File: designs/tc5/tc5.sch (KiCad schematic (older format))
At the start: 9 parts, among them J1001 SSM-104-L-SV, U1001 MCP6001-OT

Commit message: Add component for board edges, generate report
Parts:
- added BRD1: SYM_Arrow_XLarge, tc5:DemoBoard, symbol Graphic:SYM_Arrow_XLarge
- J1001: symbol Connector:Conn_01x04_Male -> tc5-rescue:Conn_01x04_Male-Connector
- QR1: symbol Graphic:SYM_Arrow_Normal -> tc5-rescue:SYM_Arrow_Normal-Graphic
- R1001: symbol Device:R_Small -> tc5-rescue:R_Small-Device
- TP1001, TP1002, TP1003, TP1004, TP1005: symbol Connector:TestPoint_Probe -> tc5-rescue:TestPoint_Probe-Connector
- U1001: symbol Amplifier_Operational:MCP6001-OT -> tc5-rescue:MCP6001-OT-Amplifier_Operational
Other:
- note added: "Symbol to represent PCB"
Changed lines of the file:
@@
 $EndDescr
 $Comp
-L Graphic:SYM_Arrow_Normal QR1
+L tc5-rescue:SYM_Arrow_Normal-Graphic QR1
 U 1 1 61C5D077
 P 1925 1450
@@
 Symbol to represent QRCode on PCB
 $Comp
-L Amplifier_Operational:MCP6001-OT U1001
+L tc5-rescue:MCP6001-OT-Amplifier_Operational U1001
 U 1 1 61C5DBDB
 P 3300 2375
@@
 $EndComp
 $Comp
-L Device:R_Small R1001
+L tc5-rescue:R_Small-Device R1001
 U 1 1 61C60726
 P 3225 3100
@@
 Connection ~ 3600 3100
 $Comp
-L Connector:Conn_01x04_Male J1001
+L tc5-rescue:Conn_01x04_Male-Connector J1001
 U 1 1 61C635DD
 P 1525 2250
@@
 	1725 2450 1950 2450
 $Comp
-L power:VCC #PWR0101
+L tc5-rescue:VCC-power #PWR0101
 U 1 1 61C66B30
 P 1950 2150
@@
 $EndComp
 $Comp
-L power:GND #PWR0102
+L tc5-rescue:GND-power #PWR0102
 U 1 1 61C67A4F
 P 1950 2250
@@
 $EndComp
 $Comp
-L power:VCC #PWR0103
+L tc5-rescue:VCC-power #PWR0103
 U 1 1 61C686E2
 P 3200 2075
@@
 $EndComp
 $Comp
-L power:GND #PWR0104
+L tc5-rescue:GND-power #PWR0104
 U 1 1 61C68E55
 P 3200 2675
@@
 _AOPIN+
 $Comp
-L Connector:TestPoint_Probe TP1003
+L tc5-rescue:TestPoint_Probe-Connector TP1003
 U 1 1 61C6D8DC
 P 4100 3100
@@
 $EndComp
 $Comp
-L Connector:TestPoint_Probe TP1002
+L tc5-rescue:TestPoint_Probe-Connector TP1002
 U 1 1 61C6F0D8
 P 2875 3100
@@
 Connection ~ 2875 3100
 $Comp
-L Connector:TestPoint_Probe TP1001
+L tc5-rescue:TestPoint_Probe-Connector TP1001
 U 1 1 61C7065D
 P 2850 2275
@@
 $EndComp
 $Comp
-L Connector:TestPoint_Probe TP1005
+L tc5-rescue:TestPoint_Probe-Connector TP1005
 U 1 1 61C76041
 P 1925 2975
@@
 $EndComp
 $Comp
-L Connector:TestPoint_Probe TP1004
+L tc5-rescue:TestPoint_Probe-Connector TP1004
 U 1 1 61C77FC1
 P 1925 2750
@@
 $EndComp
 $Comp
-L power:GND #PWR0105
+L tc5-rescue:GND-power #PWR0105
 U 1 1 61C784ED
 P 1775 2975
@@
 	1775 2975 1925 2975
 $Comp
-L power:VCC #PWR0106
+L tc5-rescue:VCC-power #PWR0106
 U 1 1 61C78DD6
 P 1775 2750
@@
 Wire Wire Line
 	1775 2750 1925 2750
+$Comp
+L Graphic:SYM_Arrow_XLarge BRD1
+U 1 1 62329410
+P 2000 1075
+F 0 "BRD1" H 2000 1165 50  0001 C CNN
+F 1 "SYM_Arrow_XLarge" H 2000 995 50  0001 C CNN
+F 2 "tc5:DemoBoard" H 2000 1075 50  0001 C CNN
+F 3 "~" H 2000 1075 50  0001 C CNN
+	1    2000 1075
+	1    0    0    -1
+$EndComp
+Text Notes 1475 975  0    50   ~ 0
+Symbol to represent PCB
 $EndSCHEMATC

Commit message: Addec TC2030 for OAR
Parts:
- added P1: TC2030, tc5:TC2030-MCP-FP, symbol Connector_Generic:Conn_02x03_Odd_Even
- added R18, R59, R60: 100k, Resistor_SMD:R_0603_1608Metric, symbol Device:R
- added TP1006: TP_HW_TYPE, TestPoint:TestPoint_Pad_D1.5mm, symbol tc5-rescue:TestPoint_Probe-Connector
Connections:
- net GND: now also R18.1, R60.1
- net VCC: now also R18.2, R59.2
- new net V_HW_TYPE: R59.1, R60.2, TP1006.1
- no-connect marks 0 -> 6
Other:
- note added: "Voltage divider to set board type"
- moved on the sheet: TP1004, TP1005

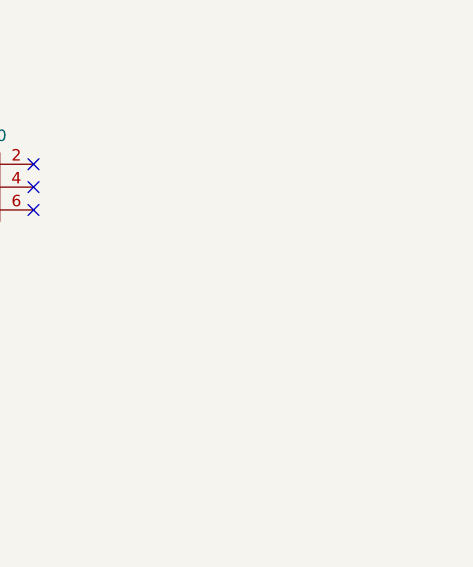
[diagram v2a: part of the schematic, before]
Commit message: Add resistors to for test
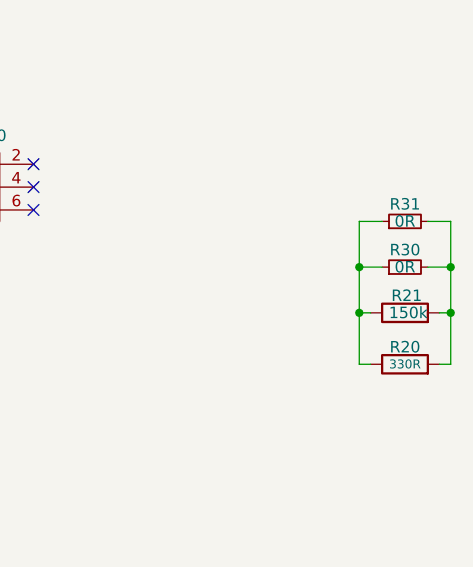
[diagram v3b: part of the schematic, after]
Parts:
- added R20: 330R, Resistor_SMD:R_0805_2012Metric, symbol Device:R
- added R21: 150k, Resistor_SMD:R_0805_2012Metric, symbol Device:R
- added R30, R31: 0R, Resistor_SMD:R_0805_2012Metric, symbol Device:R_Small
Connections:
- new net: R20.1, R21.1, R30.1, R31.1
- new net: R20.2, R21.2, R30.2, R31.2
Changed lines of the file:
@@
 	1    0    0    -1
+$EndComp
+$Comp
+L Device:R R20
+U 1 1 5F34C2CE
+P 6900 2425
+F 0 "R20" V 6975 2425 50  0000 C CNN
+F 1 "330R" V 6900 2425 39  0000 C CNN
+F 2 "Resistor_SMD:R_0805_2012Metric" H 6900 2425 50  0001 C CNN
+F 3 "~" H 6900 2425 50  0001 C CNN
+F 4 "Vishay" H 6900 2425 50  0001 C CNN "manf"
+F 5 "CRCW0603330RFKEAC" H 6900 2425 50  0001 C CNN "manf#"
+F 6 "esp32" H 6900 2425 50  0001 C CNN "variant"
+	1    6900 2425
+	0    -1   -1   0
+$EndComp
+$Comp
+L Device:R R21
+U 1 1 5DC661D7
+P 6900 2200
+F 0 "R21" V 6975 2125 50  0000 L CNN
+F 1 "150k" V 6900 2100 50  0000 L CNN
+F 2 "Resistor_SMD:R_0805_2012Metric" V 6830 2200 50  0001 C CNN
+F 3 "~" H 6900 2200 50  0001 C CNN
+F 4 "Vishay" H 6900 2200 50  0001 C CNN "manf"
+F 5 "CRCW0603150KFKEA" H 6900 2200 50  0001 C CNN "manf#"
+F 6 "RES 150k 0603" H 6900 2200 50  0001 C CNN "desc"
+	1    6900 2200
+	0    -1   -1   0
+$EndComp
+$Comp
+L Device:R_Small R30
+U 1 1 5E781FB6
+P 6900 2000
+F 0 "R30" V 6975 2000 50  0000 C CNN
+F 1 "0R" V 6900 2000 50  0000 C CNN
+F 2 "Resistor_SMD:R_0805_2012Metric" H 6900 2000 50  0001 C CNN
+F 3 "~" H 6900 2000 50  0001 C CNN
+F 4 "Vishay" H 6900 2000 50  0001 C CNN "manf"
+F 5 "CRCW04020000Z0EDC" H 6900 2000 50  0001 C CNN "manf#"
+F 6 "RES 0R 0603" H 6900 2000 50  0001 C CNN "desc"
+F 7 "connextscl_5v" H 6900 2000 50  0001 C CNN "variant"
+	1    6900 2000
+	0    -1   -1   0
+$EndComp
+$Comp
+L Device:R_Small R31
+U 1 1 5E781FC4
+P 6900 1800
+F 0 "R31" V 6975 1800 50  0000 C CNN
+F 1 "0R" V 6900 1800 50  0000 C CNN
+F 2 "Resistor_SMD:R_0805_2012Metric" H 6900 1800 50  0001 C CNN
+F 3 "~" H 6900 1800 50  0001 C CNN
+F 4 "Vishay" H 6900 1800 50  0001 C CNN "manf"
+F 5 "CRCW04020000Z0EDC" H 6900 1800 50  0001 C CNN "manf#"
+F 6 "RES 0R 0603" H 6900 1800 50  0001 C CNN "desc"
+F 7 "connextscl_3v3" H 6900 1800 50  0001 C CNN "variant"
+	1    6900 1800
+	0    -1   -1   0
 $EndComp
 NoConn ~ 4775 1550
@@
 NoConn ~ 5275 1650
 NoConn ~ 5275 1550
+Wire Wire Line
+	6750 2425 6700 2425
+Wire Wire Line
+	6700 2425 6700 2200
+Wire Wire Line
+	6700 1800 6800 1800
+Wire Wire Line
+	7050 2425 7100 2425
+Wire Wire Line
+	7100 2425 7100 2200
+Wire Wire Line
+	7100 1800 7000 1800
+Wire Wire Line
+	7050 2200 7100 2200
+Connection ~ 7100 2200
+Wire Wire Line
+	7100 2200 7100 2000
+Wire Wire Line
+	7000 2000 7100 2000
+Connection ~ 7100 2000
+Wire Wire Line
+	7100 2000 7100 1800
+Wire Wire Line
+	6800 2000 6700 2000
+Connection ~ 6700 2000
+Wire Wire Line
+	6700 2000 6700 1800
+Wire Wire Line
+	6750 2200 6700 2200
+Connection ~ 6700 2200
+Wire Wire Line
+	6700 2200 6700 2000
 $EndSCHEMATC
